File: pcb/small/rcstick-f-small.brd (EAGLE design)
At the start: 15.4 x 40 mm, 41 parts, among them J1 MOLEX_48037-0001, J2 2212S, SW1 SKRPACE010, U1 STM32F042KT, U2 CC2500, U3 MCP1703AT-3302E/CB, X1 16MHz/10pF, X2 26MHz/9pF, X3 (50 Ohm)

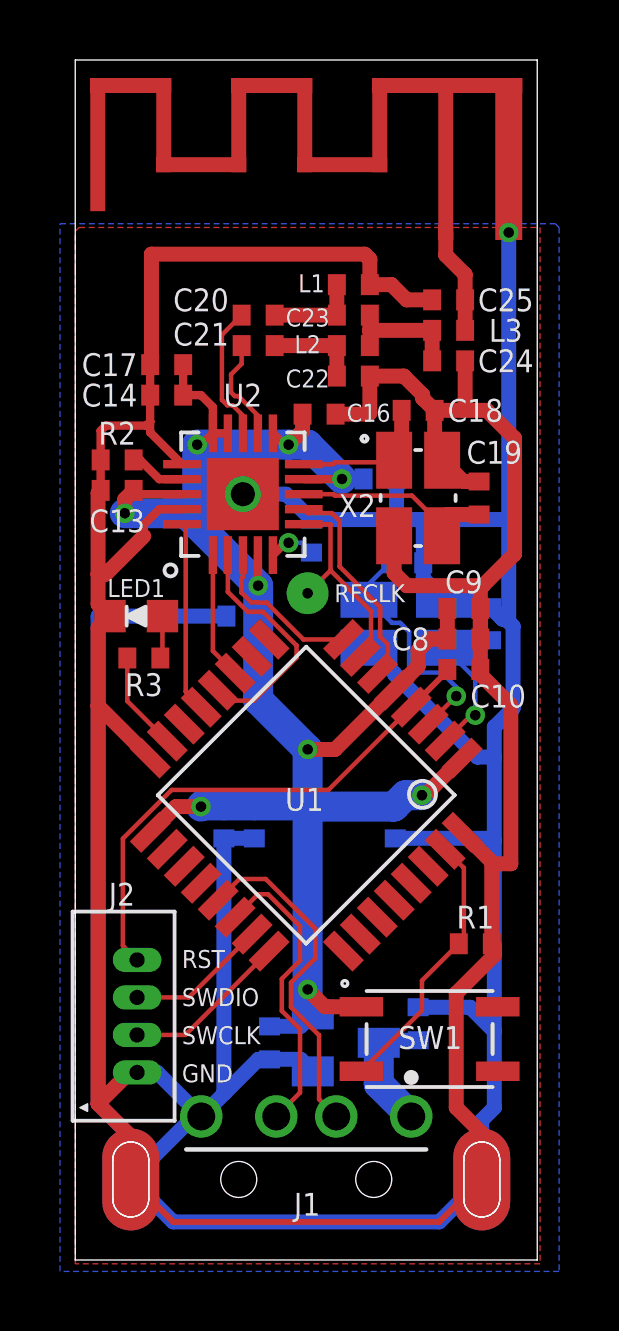
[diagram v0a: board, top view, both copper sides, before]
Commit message: add panelizing script
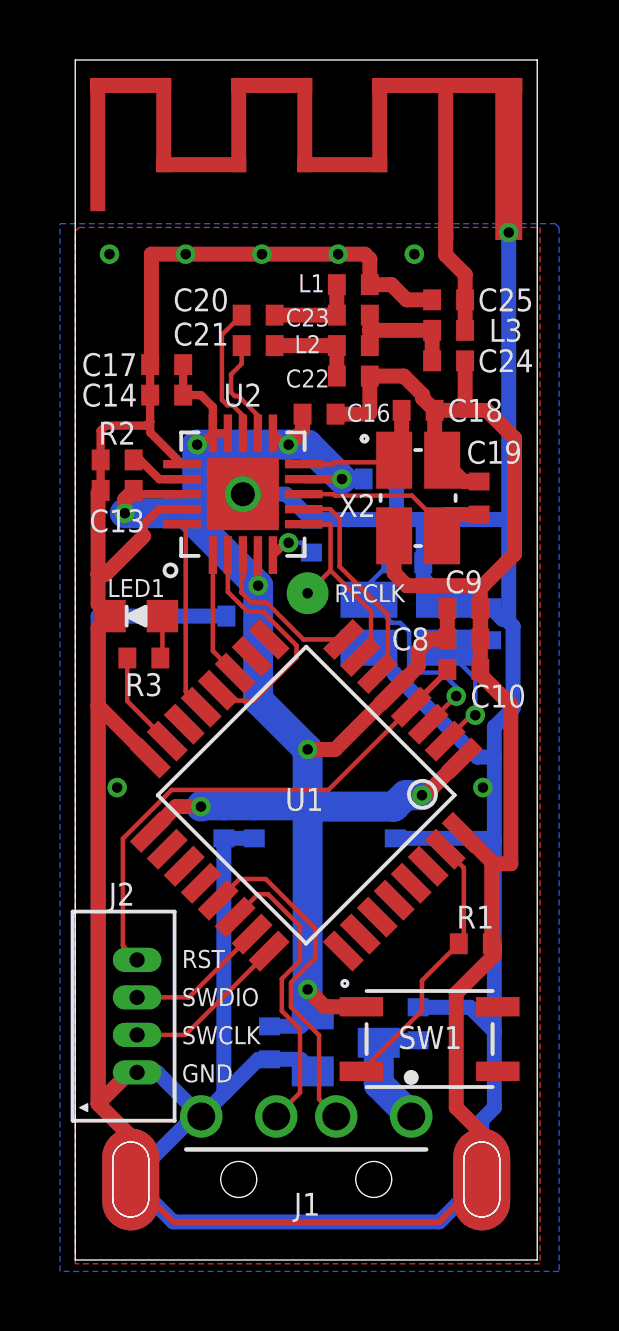
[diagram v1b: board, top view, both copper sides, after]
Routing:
- net GND: vias 0 -> 7
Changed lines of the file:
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@@
 <drawing>
 <settings>
-<setting alwaysvectorfont="yes"/>
+<setting alwaysvectorfont="no"/>
 <setting verticaltext="up"/>
 </settings>
@@
 <wire x1="1.157" y1="21.463" x2="0.762" y2="21.858" width="0.5" layer="1"/>
 <wire x1="0.762" y1="21.858" x2="0.762" y2="22.86" width="0.5" layer="1"/>
+<via x="1.143" y="33.528" extent="1-16" drill="0.35"/>
+<via x="3.683" y="33.528" extent="1-16" drill="0.35"/>
+<via x="6.223" y="33.528" extent="1-16" drill="0.35"/>
+<via x="8.763" y="33.528" extent="1-16" drill="0.35"/>
+<via x="11.303" y="33.528" extent="1-16" drill="0.35"/>
+<via x="1.397" y="15.748" extent="1-16" drill="0.35"/>
+<via x="13.589" y="15.748" extent="1-16" drill="0.35"/>
 </signal>
 <signal name="+3V3" class="2">
@@
 <contactref element="U2" pad="7"/>
 <contactref element="U1" pad="6"/>
-<wire x1="7.618" y1="25.027" x2="7.7494" y2="24.8956" width="0.1524" layer="1"/>
-<wire x1="7.7494" y1="24.8956" x2="8.55545625" y2="24.8956" width="0.1524" layer="1"/>
-<wire x1="8.55545625" y1="24.8956" x2="8.8138" y2="24.63725625" width="0.1524" layer="1"/>
-<wire x1="8.8138" y1="24.63725625" x2="8.8138" y2="23.11325625" width="0.1524" layer="1"/>
-<wire x1="8.8138" y1="23.11325625" x2="10.1638" y2="21.76325625" width="0.1524" layer="1"/>
-<wire x1="10.1638" y1="20.778103125" x2="10.424678125" y2="20.517225" width="0.1524" layer="1"/>
-<wire x1="10.424678125" y1="20.517225" x2="10.424678125" y2="19.901590625" width="0.1524" layer="1"/>
-<wire x1="10.1638" y1="21.76325625" x2="10.1638" y2="20.778103125" width="0.1524" layer="1"/>
 <wire x1="10.424678125" y1="19.901590625" x2="10.075878125" y2="19.552790625" width="0.1524" layer="1"/>
+<wire x1="7.618" y1="25.027" x2="8.501" y2="25.027" width="0.1524" layer="1"/>
+<wire x1="8.8138" y1="24.7142" x2="8.8138" y2="23.11325625" width="0.1524" layer="1"/>
+<wire x1="8.501" y1="25.027" x2="8.8138" y2="24.7142" width="0.1524" layer="1"/>
+<wire x1="8.8138" y1="23.11325625" x2="10.424678125" y2="21.502378125" width="0.1524" layer="1"/>
+<wire x1="10.424678125" y1="21.502378125" x2="10.424678125" y2="19.901590625" width="0.1524" layer="1"/>
 </signal>
 <signal name="SPI_SCK">
